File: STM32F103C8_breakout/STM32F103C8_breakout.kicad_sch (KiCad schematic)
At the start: 23 parts, among them J1 Conn_01x18_Pin, J2 Conn_01x14_Pin, J21 Conn_01x02_Pin, U1 STM32F103C8T6, U3 GPTS203211B, Y1 16 MHz Crystal

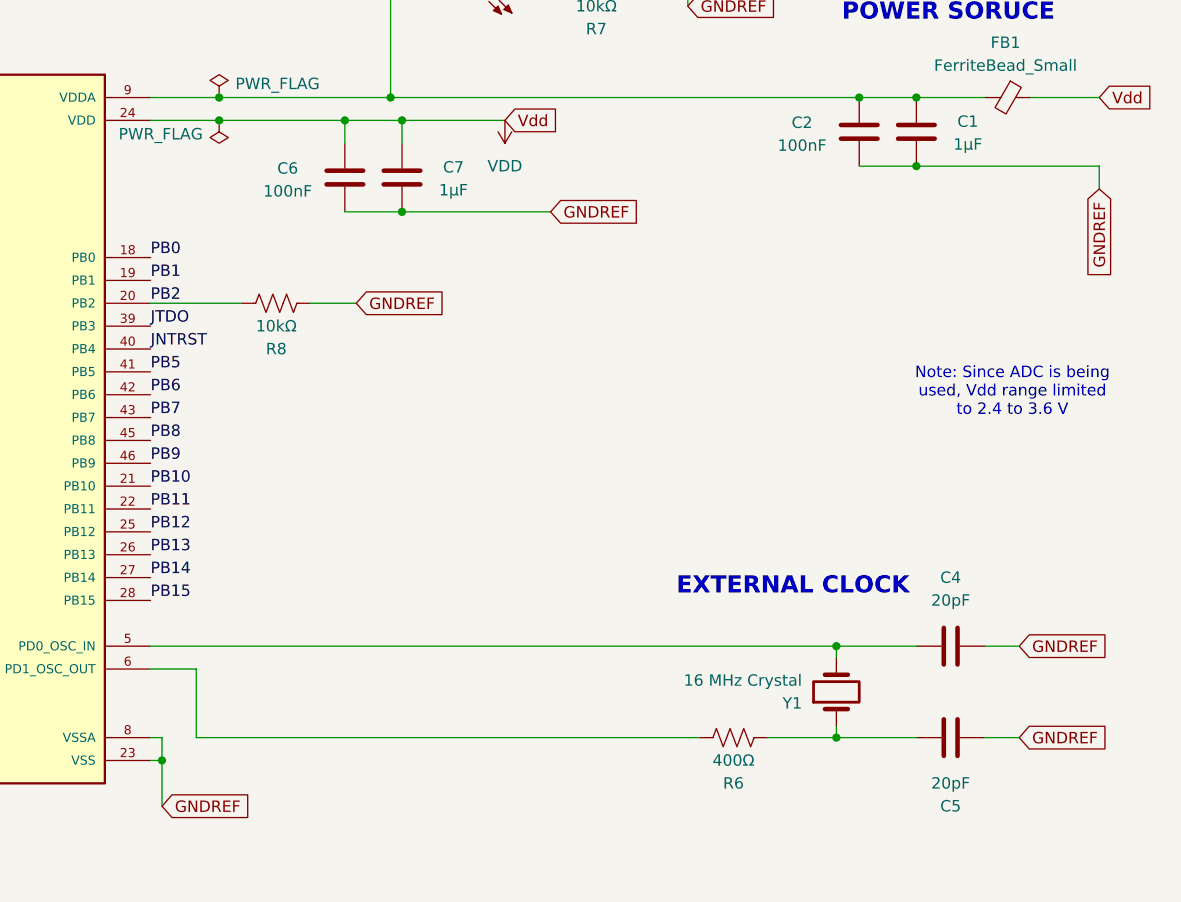
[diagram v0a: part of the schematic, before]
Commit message: Placed capacitor for battery input
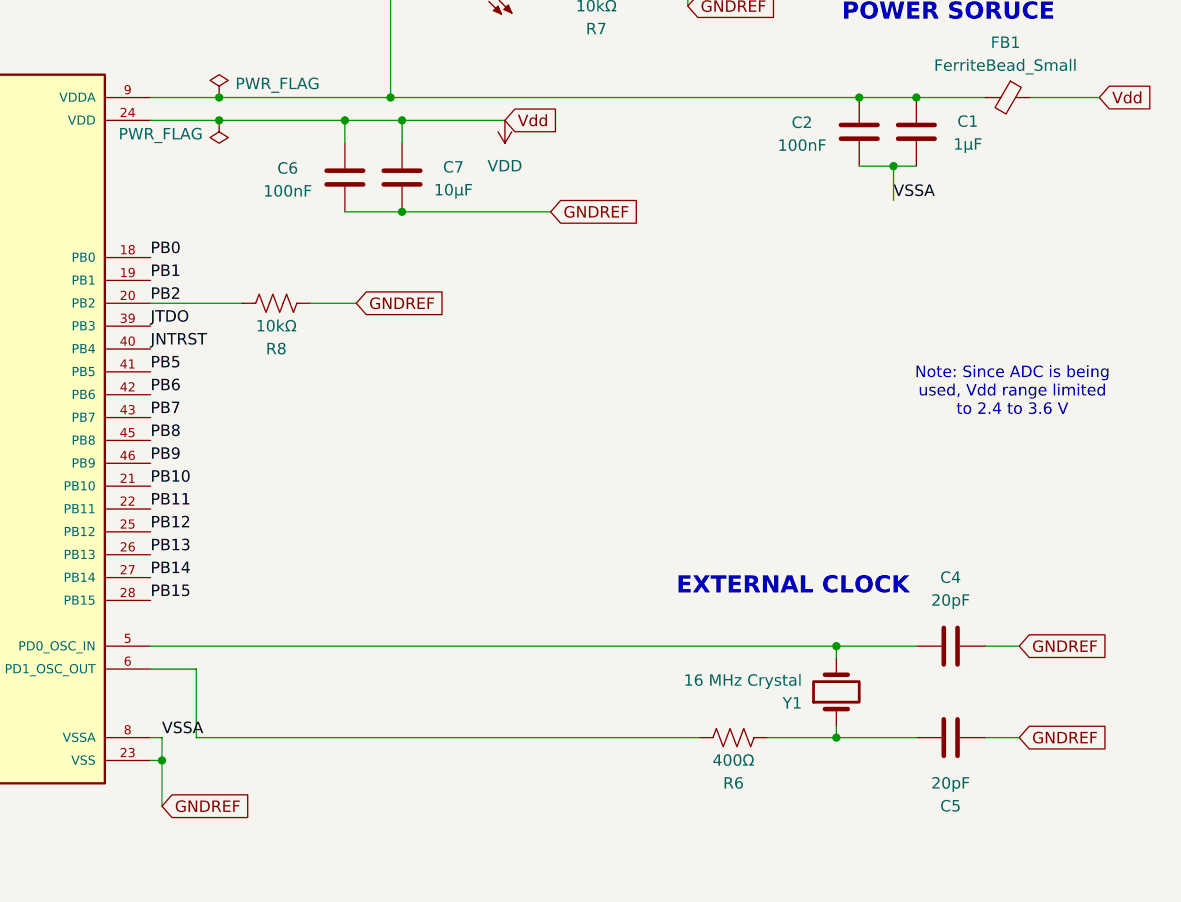
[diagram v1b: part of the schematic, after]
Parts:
- C7: value 1μF -> 10μF
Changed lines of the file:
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@@
 	)
 	(junction
-		(at 257.81 48.26)
+		(at 200.66 43.18)
 		(diameter 0)
 		(color 0 0 0 0)
 	)
 	(junction
-		(at 200.66 43.18)
+		(at 72.39 29.21)
 		(diameter 0)
 		(color 0 0 0 0)
 	)
 	(junction
-		(at 72.39 29.21)
+		(at 87.63 172.72)
 		(diameter 0)
 		(color 0 0 0 0)
 	)
 	(junction
-		(at 87.63 172.72)
+		(at 255.27 48.26)
 		(diameter 0)
 		(color 0 0 0 0)
@@
 	)
 	(junction
-		(at 173.99 114.3)
+		(at 87.63 165.1)
 		(diameter 0)
 		(color 0 0 0 0)
 	)
 	(junction
-		(at 87.63 165.1)
+		(at 180.34 43.18)
 		(diameter 0)
 		(color 0 0 0 0)
 	)
 	(junction
-		(at 180.34 43.18)
+		(at 173.99 114.3)
 		(diameter 0)
 		(color 0 0 0 0)
@@
 	(wire
 		(pts
-			(xy 82.55 170.18) (xy 87.63 170.18)
+			(xy 255.27 48.26) (xy 257.81 48.26)
 		)
 		(stroke
@@
 	(wire
 		(pts
-			(xy 172.72 40.64) (xy 180.34 40.64)
+			(xy 82.55 170.18) (xy 87.63 170.18)
 		)
 		(stroke
@@
 	(wire
 		(pts
-			(xy 248.92 102.87) (xy 248.92 101.6)
+			(xy 172.72 40.64) (xy 180.34 40.64)
 		)
 		(stroke
@@
 	(wire
 		(pts
-			(xy 30.48 154.94) (xy 57.15 154.94)
+			(xy 248.92 102.87) (xy 248.92 101.6)
 		)
 		(stroke
@@
 	(wire
 		(pts
-			(xy 87.63 165.1) (xy 87.63 167.64)
+			(xy 30.48 154.94) (xy 57.15 154.94)
 		)
 		(stroke
@@
 	(wire
 		(pts
-			(xy 49.53 186.69) (xy 49.53 190.5)
+			(xy 87.63 165.1) (xy 87.63 167.64)
 		)
 		(stroke
@@
 	(wire
 		(pts
-			(xy 257.81 48.26) (xy 278.13 48.26)
+			(xy 49.53 186.69) (xy 49.53 190.5)
 		)
 		(stroke
@@
 	(wire
 		(pts
-			(xy 251.46 48.26) (xy 257.81 48.26)
+			(xy 251.46 48.26) (xy 255.27 48.26)
 		)
 		(stroke
@@
 	(wire
 		(pts
-			(xy 278.13 48.26) (xy 278.13 50.8)
-		)
-		(stroke
-			(width 0)
-			(type default)
-		)
-	)
-	(wire
-		(pts
 			(xy 200.66 45.72) (xy 200.66 43.18)
 		)
@@
 	(wire
 		(pts
+			(xy 255.27 48.26) (xy 255.27 52.07)
+		)
+		(stroke
+			(width 0)
+			(type default)
+		)
+	)
+	(wire
+		(pts
 			(xy 199.39 27.94) (xy 199.39 40.64)
 		)
@@
 		)
 	)
+	(label "VSSA"
+		(at 173.99 111.76 0)
+		(effects
+			(font
+				(size 1.27 1.27)
+			)
+			(justify left bottom)
+		)
+	)
 	(label "PC13"
 		(at 121.92 101.6 180)
@@
 		)
 	)
+	(label "VSSA"
+		(at 255.27 52.07 0)
+		(effects
+			(font
+				(size 1.27 1.27)
+			)
+			(justify left bottom)
+		)
+	)
 	(label "PB14"
 		(at 172.72 93.98 0)
@@
 		)
 	)
-	(global_label "GNDREF"
-		(shape input)
-		(at 278.13 50.8 270)
-		(fields_autoplaced yes)
-		(effects
-			(font
-				(size 1.27 1.27)
-			)
-			(justify right)
-		)
-		(property "Intersheetrefs" "${INTERSHEET_REFS}"
-			(at 278.13 61.1633 90)
-			(hide yes)
-			(show_name no)
-			(do_not_autoplace no)
-			(effects
-				(font
-					(size 1.27 1.27)
-				)
-				(justify right)
-			)
-		)
-	)
 	(global_label "Vdd"
 		(shape input)
@@
 			)
 		)
-		(property "Value" "1μF"
+		(property "Value" "10μF"
 			(at 206.375 50.927 0)
 			(show_name no)
